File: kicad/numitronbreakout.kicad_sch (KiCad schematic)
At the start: 6 parts, among them U1 LM317_TO-220, U2 HV5812WG-G, U3 IV-12, U4 IV-12

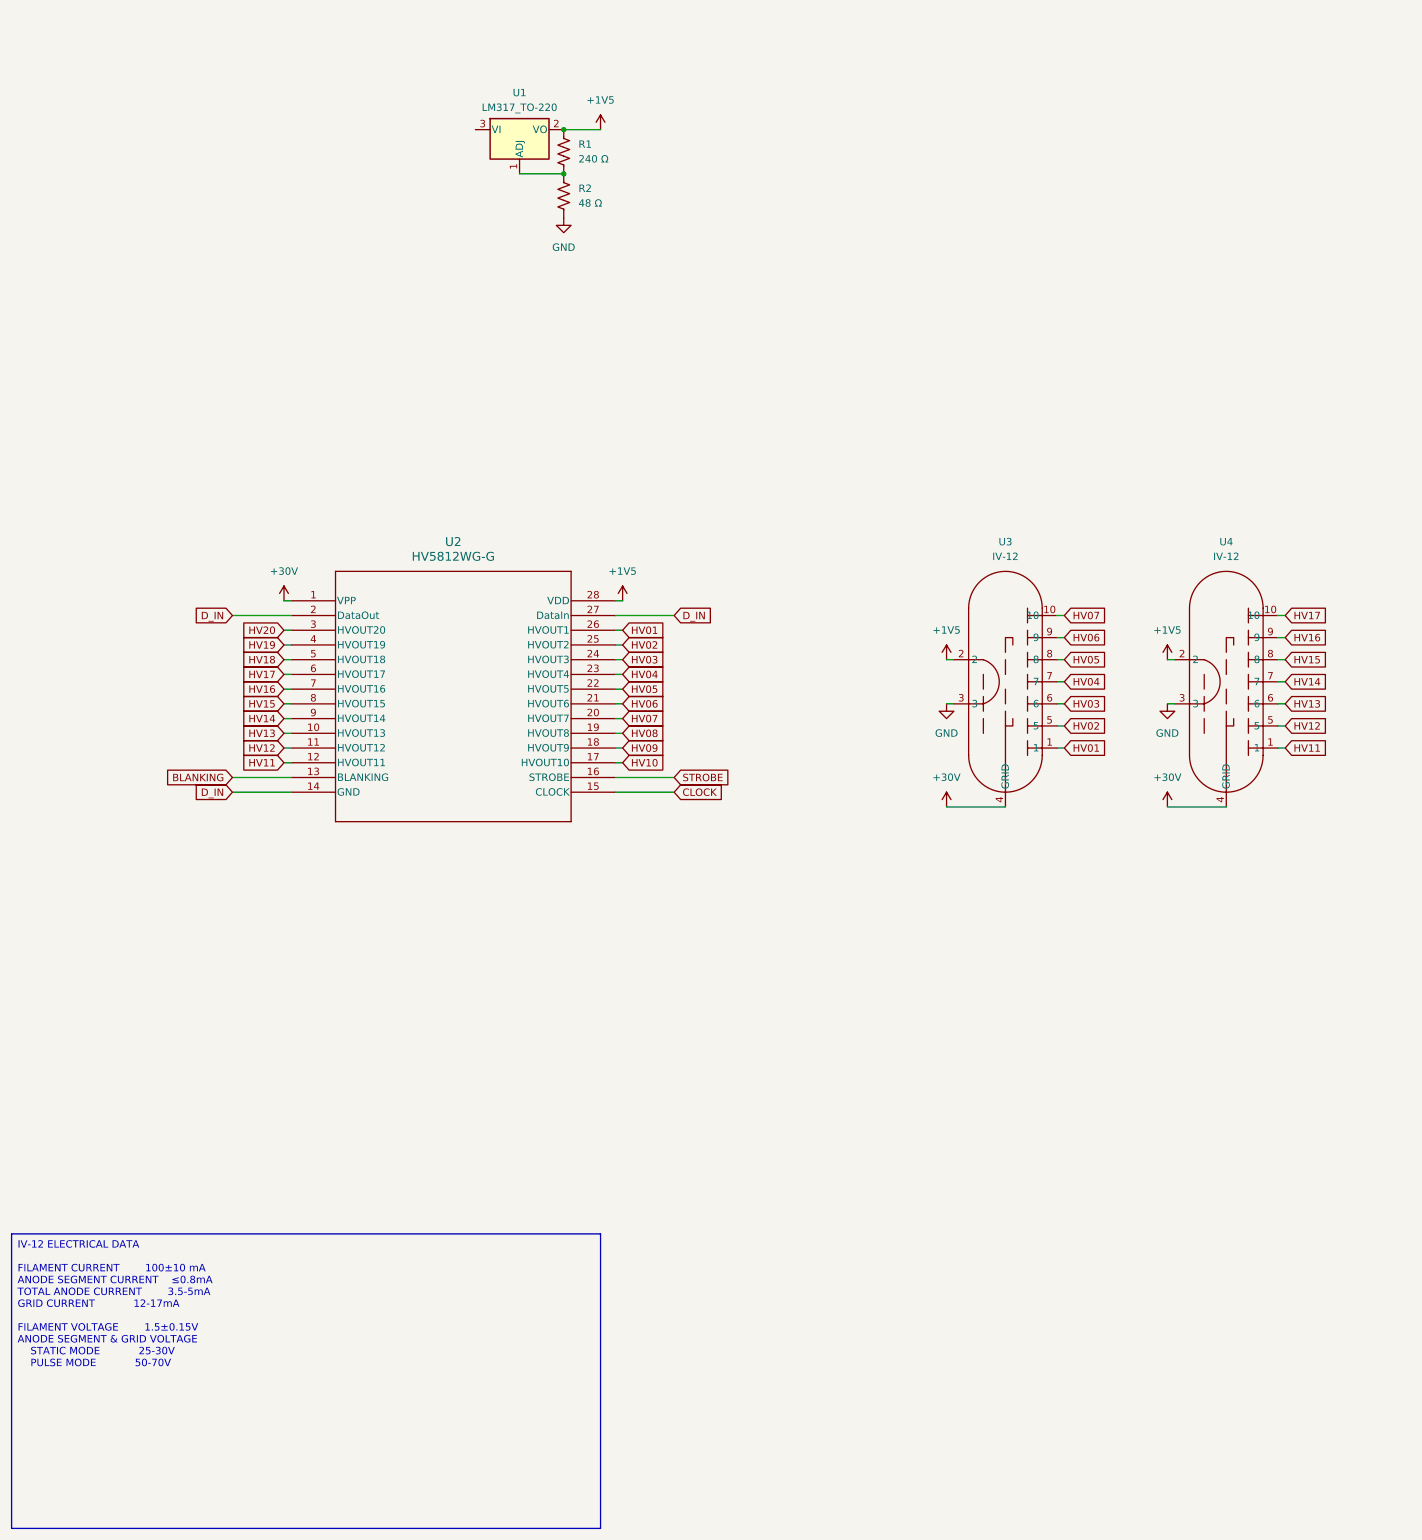
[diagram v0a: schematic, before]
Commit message: boost converter circuit populated, simplified wiring
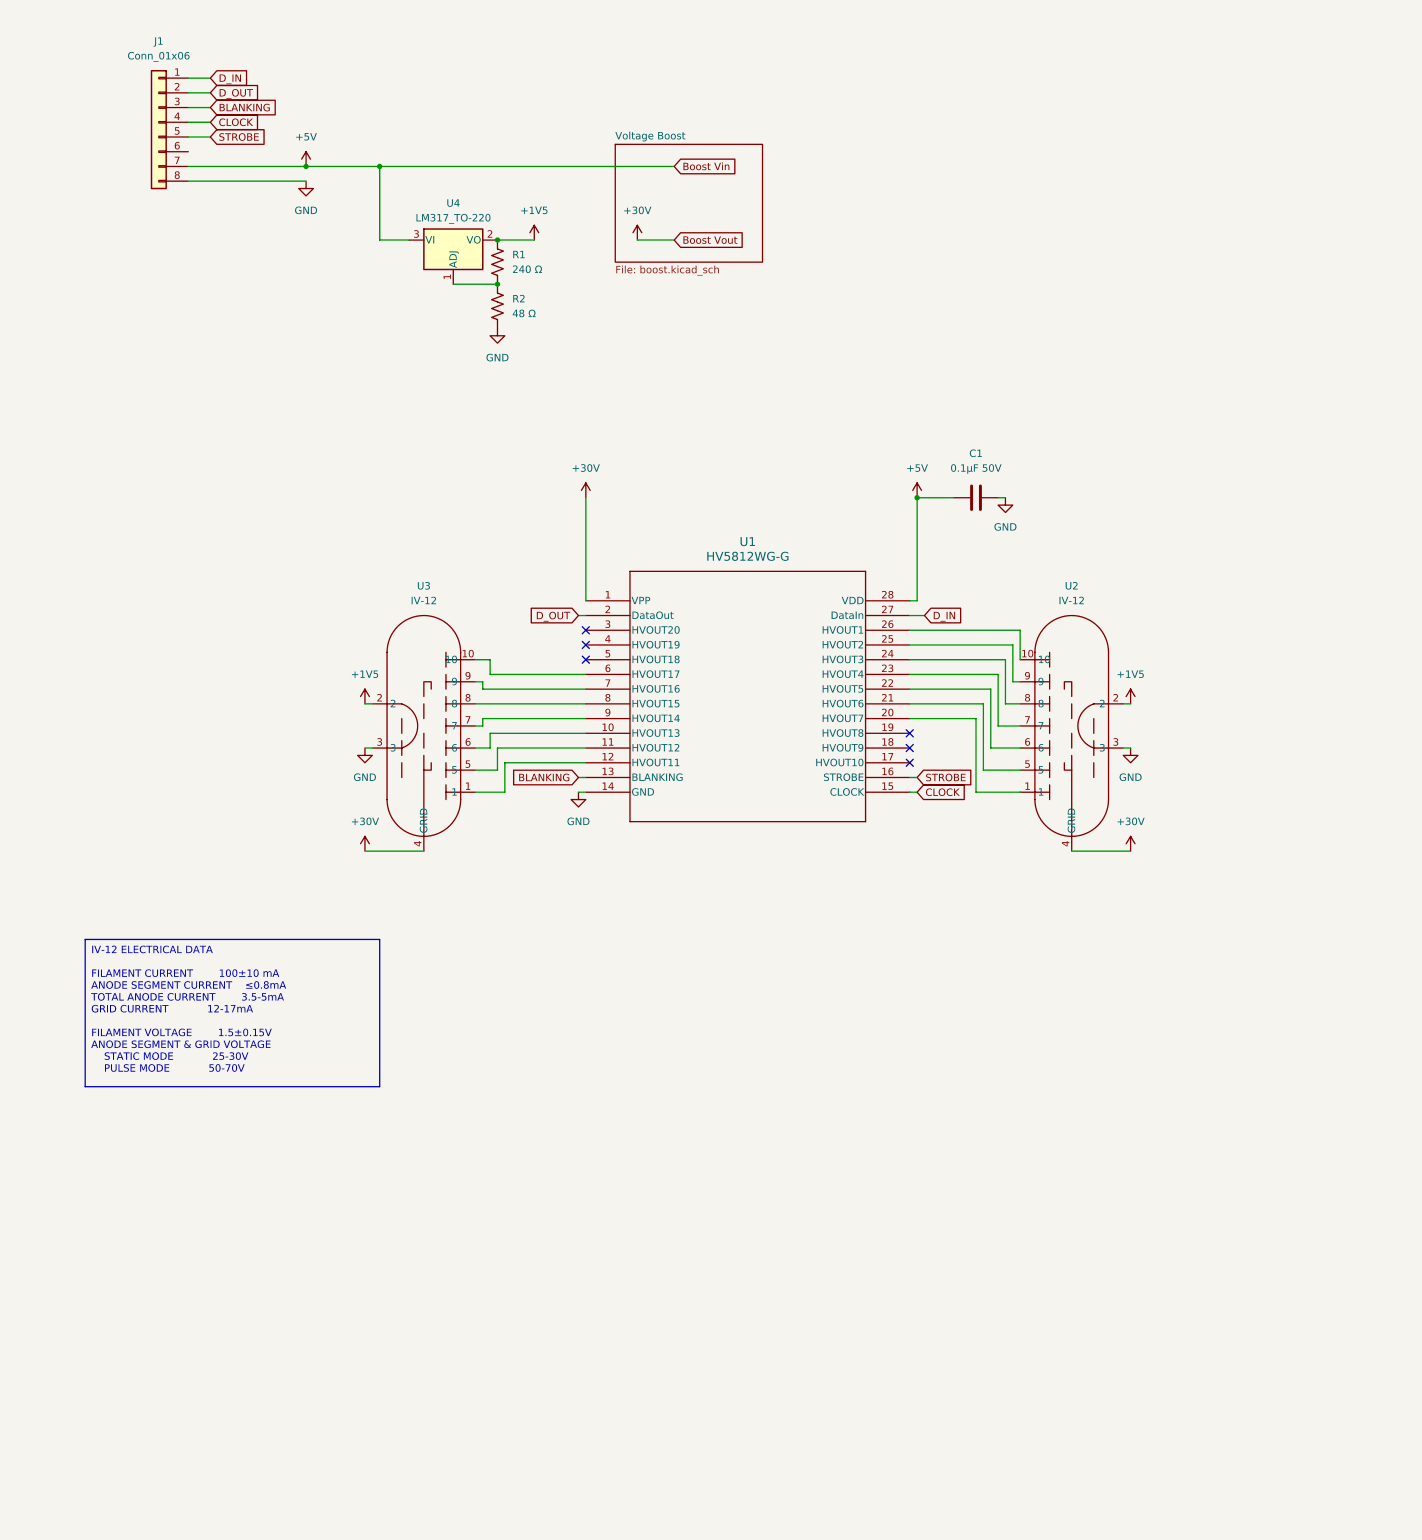
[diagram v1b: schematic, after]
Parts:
- added C1: 0.1μF 50V, symbol Device:C
- added J1: Conn_01x06, symbol Connector_Generic:Conn_01x08
- renumbered U2 to U1, U3 to U2, U4 to U3, U1 to U4
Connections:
- net +1V5: no longer U1.28 (VDD)
- net BLANKING: now also J1.3 (Pin_3)
- net CLOCK: now also J1.4 (Pin_4)
- net D_IN: now also J1.1 (Pin_1); no longer U1.14 (GND), U1.2 (DataOut)
- net GND: now also U1.14 (GND), C1.2, J1.8 (Pin_8)
- net STROBE: now also J1.5 (Pin_5)
- net +5V: now reaches U4.3 (VI)
- net +5V: now also U1.28 (VDD), C1.1, J1.7 (Pin_7)
- net HV01: no longer names the net of U2.1
- net HV01: now also U1.20 (HVOUT7); no longer U1.26 (HVOUT1)
- net HV02: no longer names the net of U2.5
- net HV02: now also U1.21 (HVOUT6); no longer U1.25 (HVOUT2)
- net HV03: no longer names the net of U2.6
- net HV03: now also U1.22 (HVOUT5); no longer U1.24 (HVOUT3)
- net HV04: no longer names the net of U1.23 (HVOUT4), U2.7
- net HV05: no longer names the net of U2.8
- net HV05: now also U1.24 (HVOUT3); no longer U1.22 (HVOUT5)
- net HV06: no longer names the net of U2.9
- net HV06: now also U1.25 (HVOUT2); no longer U1.21 (HVOUT6)
- net HV07: no longer names the net of U2.10
- net HV07: now also U1.26 (HVOUT1); no longer U1.20 (HVOUT7)
- net HV08: no longer names the net of U1.19 (HVOUT8)
- net HV09: no longer names the net of U1.18 (HVOUT9)
- net HV10: no longer names the net of U1.17 (HVOUT10)
- net HV11: no longer names the net of U1.12 (HVOUT11), U3.1
- net HV12: no longer names the net of U1.11 (HVOUT12), U3.5
- net HV13: no longer names the net of U1.10 (HVOUT13), U3.6
- net HV14: no longer names the net of U1.9 (HVOUT14), U3.7
- net HV15: no longer names the net of U1.8 (HVOUT15), U3.8
- net HV16: no longer names the net of U1.7 (HVOUT16), U3.9
- net HV17: no longer names the net of U1.6 (HVOUT17), U3.10
- net HV18: no longer names the net of U1.5 (HVOUT18)
- net HV19: no longer names the net of U1.4 (HVOUT19)
- net HV20: no longer names the net of U1.3 (HVOUT20)
- new net D_OUT: J1.2 (Pin_2), U1.2 (DataOut)
- no-connect marks 0 -> 6
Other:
- added sheet Voltage Boost (boost.kicad_sch)
- moved on the sheet: R1, R2, U1, U2, U3, U4

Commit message: library cleanup
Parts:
- U1: symbol New_Library:HV5812WG-G -> NewSymbols:HV5812WG-G
- U2, U3: symbol New_Library:IV-12 -> NewSymbols:IV-12
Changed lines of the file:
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@@
 	)
 	(symbol
-		(lib_id "New_Library:HV5812WG-G")
+		(lib_id "NewSymbols:HV5812WG-G")
 		(at 99.06 119.38 0)
 		(unit 1)
@@
 	)
 	(symbol
-		(lib_id "New_Library:IV-12")
+		(lib_id "NewSymbols:IV-12")
 		(at 71.12 140.97 270)
 		(mirror x)
@@
 	)
 	(symbol
-		(lib_id "New_Library:IV-12")
+		(lib_id "NewSymbols:IV-12")
 		(at 182.88 140.97 90)
 		(unit 1)

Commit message: began pcb layout
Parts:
- C1: footprint (none) -> Capacitor_SMD:C_1206_3216Metric_Pad1.33x1.80mm_HandSolder
- J1: footprint (none) -> Connector_PinHeader_2.54mm:PinHeader_1x08_P2.54mm_Horizontal
- R1, R2: footprint (none) -> Resistor_SMD:R_0402_1005Metric
- U1: footprint SOW28_17P90X7P50_MCH -> NewFootprints:SOW28_17P90X7P50_MCH
- U2, U3: footprint (none) -> NewFootprints:iv-12
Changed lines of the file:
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@@
 			)
 		)
-		(property "Footprint" "SOW28_17P90X7P50_MCH"
+		(property "Footprint" "NewFootprints:SOW28_17P90X7P50_MCH"
 			(at 99.06 119.38 0)
 			(effects
@@
 			)
 		)
-		(property "Footprint" ""
+		(property "Footprint" "Resistor_SMD:R_0402_1005Metric"
 			(at 84.836 68.834 90)
 			(effects
@@
 			)
 		)
-		(property "Footprint" ""
+		(property "Footprint" "Resistor_SMD:R_0402_1005Metric"
 			(at 84.836 61.214 90)
 			(effects
@@
 			)
 		)
-		(property "Footprint" ""
+		(property "Footprint" "Capacitor_SMD:C_1206_3216Metric_Pad1.33x1.80mm_HandSolder"
 			(at 170.18 100.6348 0)
 			(effects
@@
 			)
 		)
-		(property "Footprint" ""
+		(property "Footprint" "NewFootprints:iv-12"
 			(at 71.12 140.97 0)
 			(effects
@@
 			)
 		)
-		(property "Footprint" ""
+		(property "Footprint" "Connector_PinHeader_2.54mm:PinHeader_1x08_P2.54mm_Horizontal"
 			(at 25.4 36.83 0)
 			(effects
@@
 			)
 		)
-		(property "Footprint" ""
+		(property "Footprint" "NewFootprints:iv-12"
 			(at 182.88 140.97 0)
 			(effects
